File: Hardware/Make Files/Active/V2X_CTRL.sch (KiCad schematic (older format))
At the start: 37 parts, among them CON1 AVR-PDI-6, IC1 ATXMEGA16A4U-A, P20 Jumper 1, P21 Jumper 2, P22 CONN_02X04, P23 Jumper 3, P24 Jumper 4, Q16 2N7000, Q17 2N7000, Q18 2N7000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

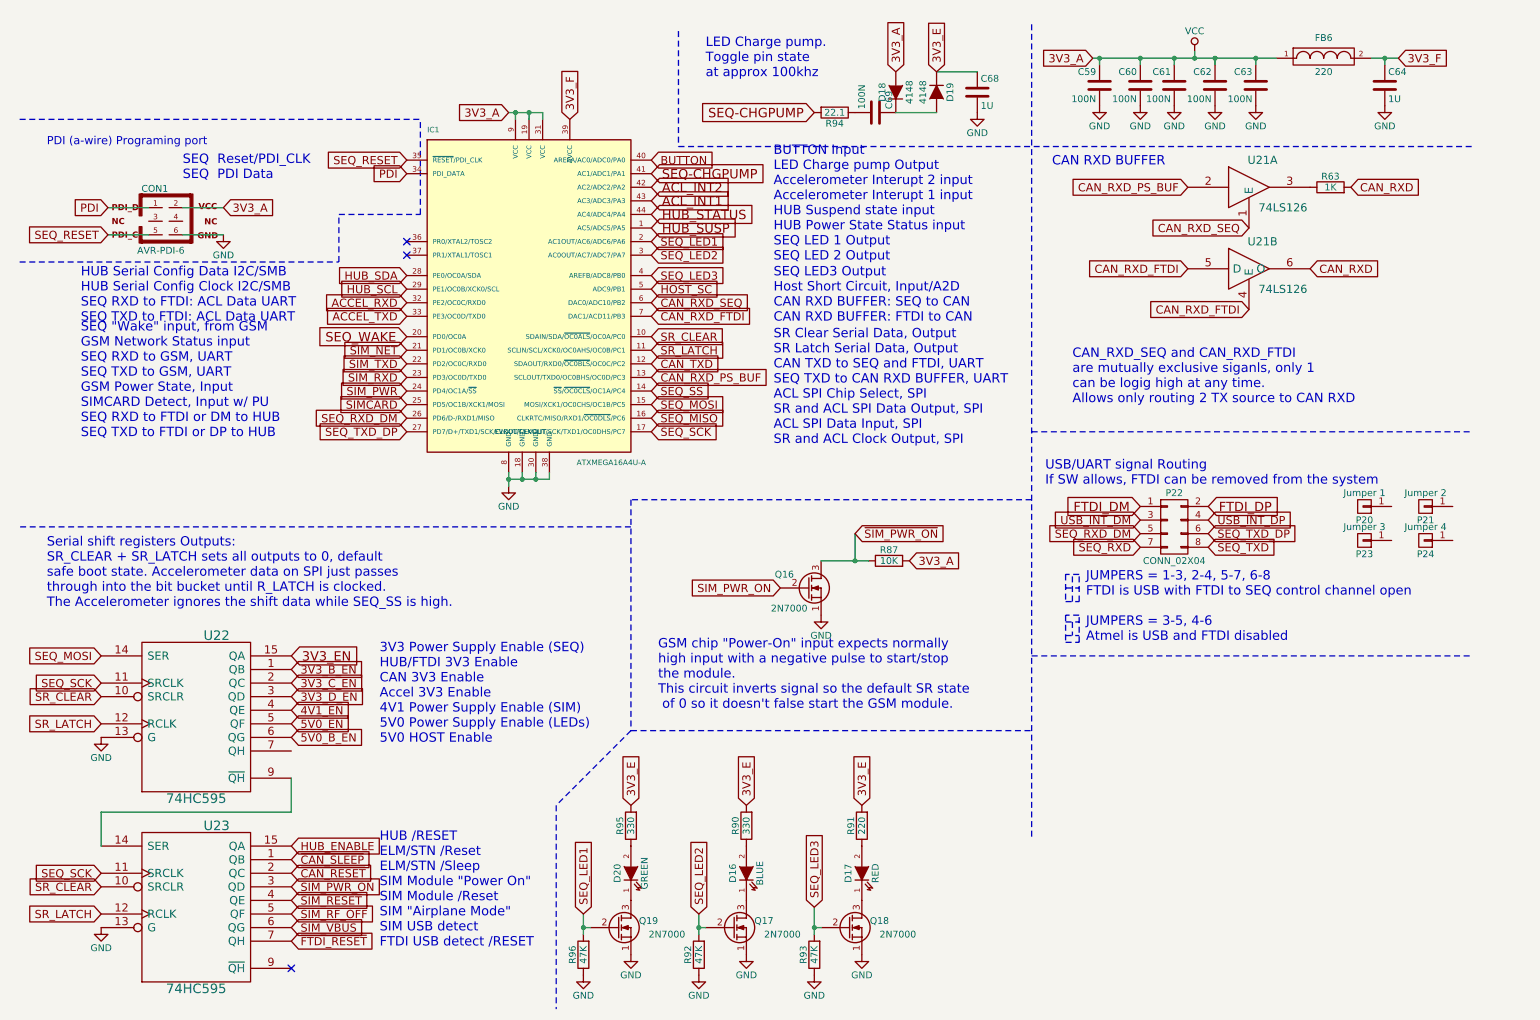
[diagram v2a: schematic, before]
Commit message: Verification findings and modifications
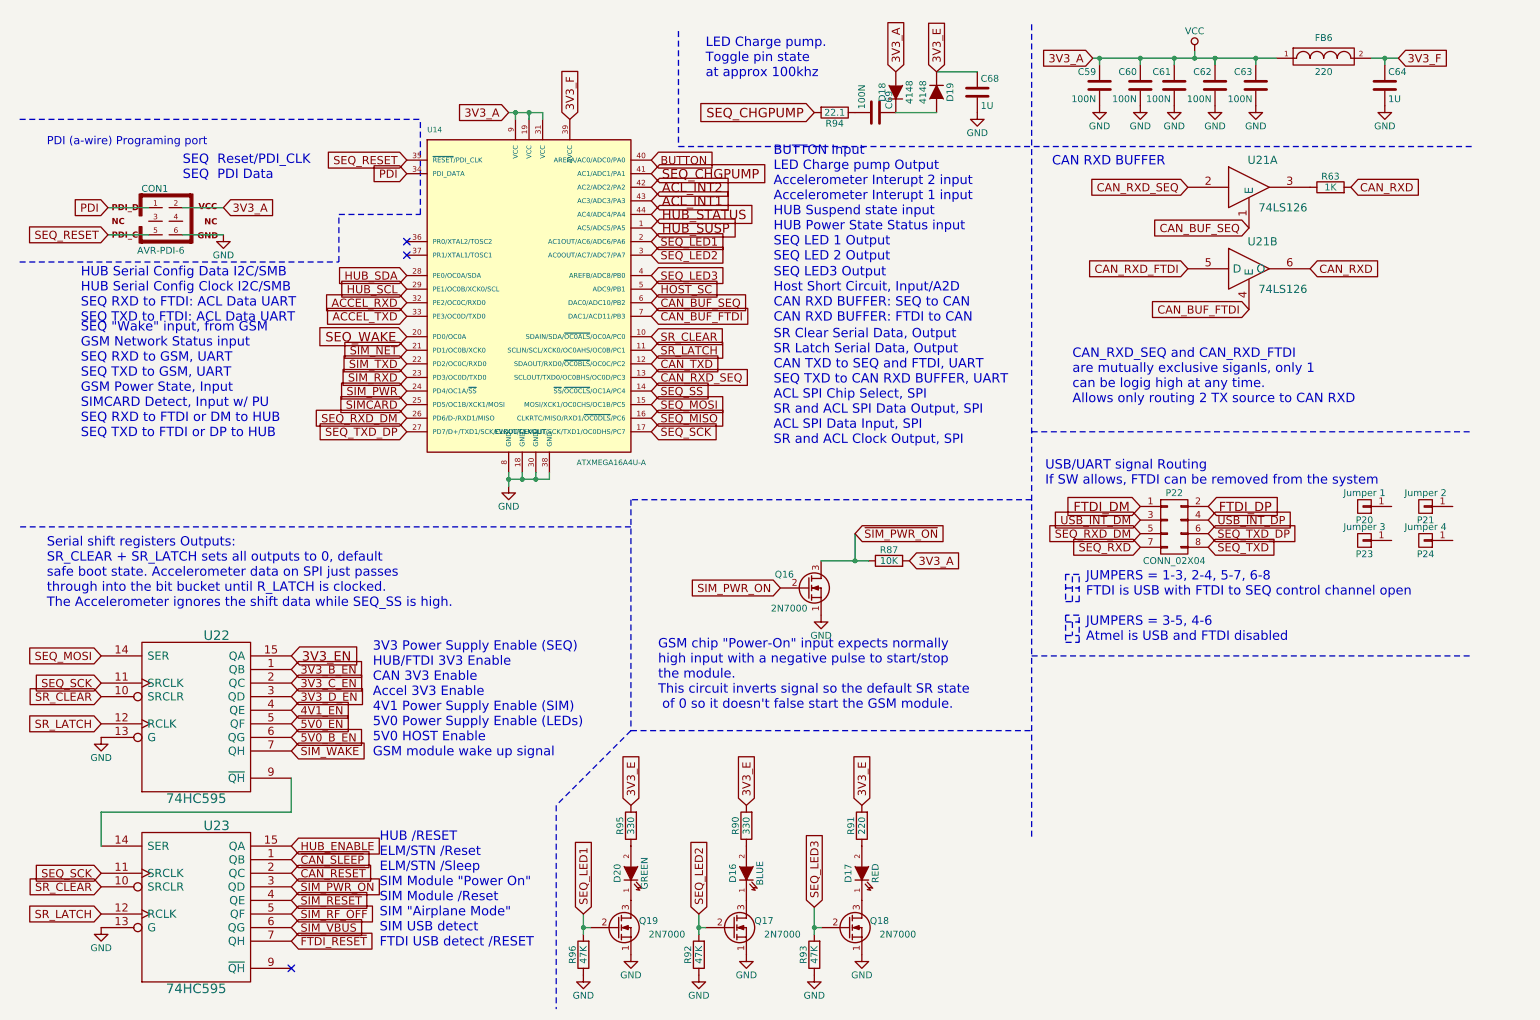
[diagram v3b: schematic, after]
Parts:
- CON1: footprint Pin_Headers:Pin_Header_Straight_2x03 -> Pin_Headers:Pin_Header_Angled_2x03
- renumbered IC1 to U14
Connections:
- net CAN_RXD_PS_BUF is gone; now on net CAN_RXD_SEQ: U14.13 (SCLOUT/TXD0/OC0BHS/OC0D/PC3), U21.2
- net CAN_RXD_FTDI: no longer U14.7 (DAC1/ACD11/PB3), U21.4 (E)
- net CAN_RXD_SEQ: no longer U14.6 (DAC0/ADC10/PB2), U21.1 (E)
- net SIM_WAKE: now reaches U22.7 (QH)
- net SEQ-CHGPUMP renamed SEQ_CHGPUMP
- new net CAN_BUF_FTDI: U14.7 (DAC1/ACD11/PB3), U21.4 (E)
- new net CAN_BUF_SEQ: U14.6 (DAC0/ADC10/PB2), U21.1 (E)
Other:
- note added: "3V3 Power Supply Enable (SEQ)\nHUB/FTDI 3V3 Enable\nCAN 3V3 Enable\nAccel 3V3 Enable\n4V1 Power Supply Enable (SIM)\n5V0 Power Supply Enable (LEDs)\n5V0 HOST Enable \nGSM module wake up signal"
- note removed: "3V3 Power Supply Enable (SEQ)\nHUB/FTDI 3V3 Enable\nCAN 3V3 Enable\nAccel 3V3 Enable\n4V1 Power Supply Enable (SIM)\n5V0 Power Supply Enable (LEDs)\n5V0 HOST Enable \n"
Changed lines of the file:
@@
 SEQ_LED2
 $Comp
-L GND #PWR96
+L GND #PWR092
 U 1 1 55F86E9C
 P 4100 3900
-F 0 "#PWR96" H 4100 3650 50  0001 C CNN
+F 0 "#PWR092" H 4100 3650 50  0001 C CNN
 F 1 "GND" H 4100 3750 50  0000 C CNN
 F 2 "" H 4100 3900 60  0000 C CNN
@@
 HOST_SC
 $Comp
-L ATXMEGA16A4U-A IC1
+L ATXMEGA16A4U-A U14
 U 1 1 55F86EE3
 P 4250 2500
-F 0 "IC1" H 3500 3700 40  0000 L BNN
+F 0 "U14" H 3500 3700 40  0000 L BNN
 F 1 "ATXMEGA16A4U-A" H 4600 1250 40  0000 L BNN
 F 2 "Housings_QFP:TQFP-44_10x10mm_Pitch0.8mm" H 4250 2500 35  0001 C CIN
@@
 PDI
 $Comp
-L GND #PWR95
+L GND #PWR093
 U 1 1 55F86EF0
 P 2000 2050
-F 0 "#PWR95" H 2000 1800 50  0001 C CNN
+F 0 "#PWR093" H 2000 1800 50  0001 C CNN
 F 1 "GND" H 2000 1900 50  0000 C CNN
 F 2 "" H 2000 2050 60  0000 C CNN
@@
 F 0 "CON1" H 1495 2190 50  0000 C CNN
 F 1 "AVR-PDI-6" H 1365 1705 50  0000 L BNN
-F 2 "Pin_Headers:Pin_Header_Straight_2x03" V 1130 1985 50  0001 C CNN
+F 2 "Pin_Headers:Pin_Header_Angled_2x03" V 1130 1985 50  0001 C CNN
 F 3 "http://www.mouser.com/ds/2/418/NG_CD_146130_L_146130_c.dwg-614944.pdf" H 1575 1950 60  0001 C CNN
 F 4 "571-5-146130-2" H 1575 1950 60  0001 C CNN "Mouse PN"
@@
 Text Notes 3150 7300 0    69   ~ 0
 HUB /RESET\nELM/STN /Reset\nELM/STN /Sleep\nSIM Module "Power On"\nSIM Module /Reset\nSIM "Airplane Mode"\nSIM USB detect\nFTDI USB detect /RESET
-Text Notes 3150 5800 0    69   ~ 0
-3V3 Power Supply Enable (SEQ)\nHUB/FTDI 3V3 Enable\nCAN 3V3 Enable\nAccel 3V3 Enable\n4V1 Power Supply Enable (SIM)\n5V0 Power Supply Enable (LEDs)\n5V0 HOST Enable \n
+Text Notes 3100 5900 0    69   ~ 0
+3V3 Power Supply Enable (SEQ)\nHUB/FTDI 3V3 Enable\nCAN 3V3 Enable\nAccel 3V3 Enable\n4V1 Power Supply Enable (SIM)\n5V0 Power Supply Enable (LEDs)\n5V0 HOST Enable \nGSM module wake up signal
 Text Notes 950  2700 0    69   ~ 0
 HUB Serial Config Data I2C/SMB\nHUB Serial Config Clock I2C/SMB\nSEQ RXD to FTDI: ACL Data UART\nSEQ TXD to FTDI: ACL Data UART
@@
 $EndComp
 Text GLabel 9100 1700 0    60   Input ~ 0
-CAN_RXD_PS_BUF
+CAN_RXD_SEQ
 Text GLabel 9100 2300 0    60   Input ~ 0
 CAN_RXD_FTDI
@@
 5V0_B_EN
 $Comp
-L GND #PWR93
+L GND #PWR094
 U 1 1 55FA434A
 P 1100 5750
-F 0 "#PWR93" H 1100 5500 50  0001 C CNN
+F 0 "#PWR094" H 1100 5500 50  0001 C CNN
 F 1 "GND" H 1100 5600 50  0000 C CNN
 F 2 "" H 1100 5750 60  0000 C CNN
@@
 $EndComp
 $Comp
-L GND #PWR94
+L GND #PWR095
 U 1 1 55FA46C8
 P 1100 7150
-F 0 "#PWR94" H 1100 6900 50  0001 C CNN
+F 0 "#PWR095" H 1100 6900 50  0001 C CNN
 F 1 "GND" H 1100 7000 50  0000 C CNN
 F 2 "" H 1100 7150 60  0000 C CNN
@@
 $EndComp
 $Comp
-L GND #PWR100
+L GND #PWR096
 U 1 1 55FD726F
 P 5850 7350
-F 0 "#PWR100" H 5850 7100 50  0001 C CNN
+F 0 "#PWR096" H 5850 7100 50  0001 C CNN
 F 1 "GND" H 5850 7200 50  0000 C CNN
 F 2 "" H 5850 7350 60  0000 C CNN
@@
 $EndComp
 $Comp
-L GND #PWR99
+L GND #PWR097
 U 1 1 55FD7284
 P 5500 7500
-F 0 "#PWR99" H 5500 7250 50  0001 C CNN
+F 0 "#PWR097" H 5500 7250 50  0001 C CNN
 F 1 "GND" H 5500 7350 50  0000 C CNN
 F 2 "" H 5500 7500 60  0000 C CNN
@@
 $EndComp
 $Comp
-L GND #PWR101
+L GND #PWR098
 U 1 1 55FD7672
 P 6350 7500
-F 0 "#PWR101" H 6350 7250 50  0001 C CNN
+F 0 "#PWR098" H 6350 7250 50  0001 C CNN
 F 1 "GND" H 6350 7350 50  0000 C CNN
 F 2 "" H 6350 7500 60  0000 C CNN
@@
 	6350 7000 6350 7200
 $Comp
-L GND #PWR103
+L GND #PWR099
 U 1 1 55FD7660
 P 6700 7350
-F 0 "#PWR103" H 6700 7100 50  0001 C CNN
+F 0 "#PWR099" H 6700 7100 50  0001 C CNN
 F 1 "GND" H 6700 7200 50  0000 C CNN
 F 2 "" H 6700 7350 60  0000 C CNN
@@
 $EndComp
 $Comp
-L GND #PWR102
+L GND #PWR0100
 U 1 1 55FE1020
 P 6400 4850
-F 0 "#PWR102" H 6400 4600 50  0001 C CNN
+F 0 "#PWR0100" H 6400 4600 50  0001 C CNN
 F 1 "GND" H 6400 4700 50  0000 C CNN
 F 2 "" H 6400 4850 60  0000 C CNN
@@
 Connection ~ 10550 750
 $Comp
-L GND #PWR111
+L GND #PWR0101
 U 1 1 56006FBB
 P 10550 1100
-F 0 "#PWR111" H 10550 850 50  0001 C CNN
+F 0 "#PWR0101" H 10550 850 50  0001 C CNN
 F 1 "GND" H 10550 950 50  0000 C CNN
 F 2 "" H 10550 1100 60  0000 C CNN
@@
 Connection ~ 9000 750
 $Comp
-L GND #PWR107
+L GND #PWR0102
 U 1 1 560285A0
 P 9000 1100
-F 0 "#PWR107" H 9000 850 50  0001 C CNN
+F 0 "#PWR0102" H 9000 850 50  0001 C CNN
 F 1 "GND" H 9000 950 50  0000 C CNN
 F 2 "" H 9000 1100 60  0000 C CNN
@@
 $EndComp
 $Comp
-L GND #PWR109
+L GND #PWR0103
 U 1 1 560285F6
 P 9300 1100
-F 0 "#PWR109" H 9300 850 50  0001 C CNN
+F 0 "#PWR0103" H 9300 850 50  0001 C CNN
 F 1 "GND" H 9300 950 50  0000 C CNN
 F 2 "" H 9300 1100 60  0000 C CNN
@@
 $EndComp
 $Comp
-L GND #PWR110
+L GND #PWR0104
 U 1 1 5602864C
 P 9600 1100
-F 0 "#PWR110" H 9600 850 50  0001 C CNN
+F 0 "#PWR0104" H 9600 850 50  0001 C CNN
 F 1 "GND" H 9600 950 50  0000 C CNN
 F 2 "" H 9600 1100 60  0000 C CNN
@@
 Connection ~ 9150 750
 $Comp
-L VCC #PWR108
+L VCC #PWR0105
 U 1 1 56029609
 P 9150 700
-F 0 "#PWR108" H 9150 550 50  0001 C CNN
+F 0 "#PWR0105" H 9150 550 50  0001 C CNN
 F 1 "VCC" H 9150 850 50  0000 C CNN
 F 2 "" H 9150 700 60  0000 C CNN
@@
 Connection ~ 8750 750
 $Comp
-L GND #PWR106
+L GND #PWR0106
 U 1 1 5602C4DB
 P 8750 1100
-F 0 "#PWR106" H 8750 850 50  0001 C CNN
+F 0 "#PWR0106" H 8750 850 50  0001 C CNN
 F 1 "GND" H 8750 950 50  0000 C CNN
 F 2 "" H 8750 1100 60  0000 C CNN
@@
 $EndComp
 $Comp
-L GND #PWR105
+L GND #PWR0107
 U 1 1 5602C537
 P 8450 1100
-F 0 "#PWR105" H 8450 850 50  0001 C CNN
+F 0 "#PWR0107" H 8450 850 50  0001 C CNN
 F 1 "GND" H 8450 950 50  0000 C CNN
 F 2 "" H 8450 1100 60  0000 C CNN
@@
 3V3_A
 Text GLabel 9550 2600 0    60   Input ~ 0
-CAN_RXD_FTDI
+CAN_BUF_FTDI
 Text GLabel 9550 2000 0    60   Input ~ 0
-CAN_RXD_SEQ
+CAN_BUF_SEQ
 Text GLabel 2500 5450 2    60   Input ~ 0
 3V3_D_EN
-Text GLabel 5150 2550 2    60   Input ~ 0
-CAN_RXD_SEQ
-Text GLabel 5150 2650 2    60   Input ~ 0
-CAN_RXD_FTDI
 Text GLabel 8750 4150 0    60   Input ~ 0
 USB_INT_DM
@@
 SEQ_LED3
 Text GLabel 5150 1600 2    69   Input ~ 0
-SEQ-CHGPUMP
+SEQ_CHGPUMP
 $Comp
 L LED D20
@@
 $EndComp
 $Comp
-L GND #PWR98
+L GND #PWR0108
 U 1 1 560D95B8
 P 5000 7350
-F 0 "#PWR98" H 5000 7100 50  0001 C CNN
+F 0 "#PWR0108" H 5000 7100 50  0001 C CNN
 F 1 "GND" H 5000 7200 50  0000 C CNN
 F 2 "" H 5000 7350 60  0000 C CNN
@@
 $EndComp
 $Comp
-L GND #PWR97
+L GND #PWR0109
 U 1 1 560D95C5
 P 4650 7500
-F 0 "#PWR97" H 4650 7250 50  0001 C CNN
+F 0 "#PWR0109" H 4650 7250 50  0001 C CNN
 F 1 "GND" H 4650 7350 50  0000 C CNN
 F 2 "" H 4650 7500 60  0000 C CNN
@@
 $EndComp
 Text GLabel 6350 1150 0    69   Input ~ 0
-SEQ-CHGPUMP
+SEQ_CHGPUMP
 $Comp
 L R R94
@@
 $EndComp
 $Comp
-L GND #PWR104
+L GND #PWR0110
 U 1 1 560DBE9F
 P 7550 1150
-F 0 "#PWR104" H 7550 900 50  0001 C CNN
+F 0 "#PWR0110" H 7550 900 50  0001 C CNN
 F 1 "GND" H 7550 1000 50  0000 C CNN
 F 2 "" H 7550 1150 60  0000 C CNN
@@
 Text GLabel 6350 7000 1    60   Input ~ 0
 SEQ_LED3
-Text GLabel 5150 3100 2    60   Input ~ 0
-CAN_RXD_PS_BUF
 Text Notes 8100 1550 0    69   ~ 0
 CAN RXD BUFFER
@@
 	0    -1   -1   0
 $EndComp
+Text GLabel 5150 2550 2    60   Input ~ 0
+CAN_BUF_SEQ
+Text GLabel 5150 2650 2    60   Input ~ 0
+CAN_BUF_FTDI
+Text GLabel 5150 3100 2    60   Input ~ 0
+CAN_RXD_SEQ
+Text GLabel 2500 5850 2    60   Input ~ 0
+SIM_WAKE
 $EndSCHEMATC

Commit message: V2X V1.2 PCB build, with shares
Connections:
- no-connect marks 3 -> 9
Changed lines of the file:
@@
 SEQ_LED2
 $Comp
-L GND #PWR092
+L GND #PWR094
 U 1 1 55F86E9C
 P 4100 3900
-F 0 "#PWR092" H 4100 3650 50  0001 C CNN
+F 0 "#PWR094" H 4100 3650 50  0001 C CNN
 F 1 "GND" H 4100 3750 50  0000 C CNN
 F 2 "" H 4100 3900 60  0000 C CNN
@@
 PDI
 $Comp
-L GND #PWR093
+L GND #PWR095
 U 1 1 55F86EF0
 P 2000 2050
-F 0 "#PWR093" H 2000 1800 50  0001 C CNN
+F 0 "#PWR095" H 2000 1800 50  0001 C CNN
 F 1 "GND" H 2000 1900 50  0000 C CNN
 F 2 "" H 2000 2050 60  0000 C CNN
@@
 5V0_B_EN
 $Comp
-L GND #PWR094
+L GND #PWR096
 U 1 1 55FA434A
 P 1100 5750
-F 0 "#PWR094" H 1100 5500 50  0001 C CNN
+F 0 "#PWR096" H 1100 5500 50  0001 C CNN
 F 1 "GND" H 1100 5600 50  0000 C CNN
 F 2 "" H 1100 5750 60  0000 C CNN
@@
 $EndComp
 $Comp
-L GND #PWR095
+L GND #PWR097
 U 1 1 55FA46C8
 P 1100 7150
-F 0 "#PWR095" H 1100 6900 50  0001 C CNN
+F 0 "#PWR097" H 1100 6900 50  0001 C CNN
 F 1 "GND" H 1100 7000 50  0000 C CNN
 F 2 "" H 1100 7150 60  0000 C CNN
@@
 $EndComp
 $Comp
-L GND #PWR096
+L GND #PWR098
 U 1 1 55FD726F
 P 5850 7350
-F 0 "#PWR096" H 5850 7100 50  0001 C CNN
+F 0 "#PWR098" H 5850 7100 50  0001 C CNN
 F 1 "GND" H 5850 7200 50  0000 C CNN
 F 2 "" H 5850 7350 60  0000 C CNN
@@
 $EndComp
 $Comp
-L GND #PWR097
+L GND #PWR099
 U 1 1 55FD7284
 P 5500 7500
-F 0 "#PWR097" H 5500 7250 50  0001 C CNN
+F 0 "#PWR099" H 5500 7250 50  0001 C CNN
 F 1 "GND" H 5500 7350 50  0000 C CNN
 F 2 "" H 5500 7500 60  0000 C CNN
@@
 $EndComp
 $Comp
-L GND #PWR098
+L GND #PWR0100
 U 1 1 55FD7672
 P 6350 7500
-F 0 "#PWR098" H 6350 7250 50  0001 C CNN
+F 0 "#PWR0100" H 6350 7250 50  0001 C CNN
 F 1 "GND" H 6350 7350 50  0000 C CNN
 F 2 "" H 6350 7500 60  0000 C CNN
@@
 	6350 7000 6350 7200
 $Comp
-L GND #PWR099
+L GND #PWR0101
 U 1 1 55FD7660
 P 6700 7350
-F 0 "#PWR099" H 6700 7100 50  0001 C CNN
+F 0 "#PWR0101" H 6700 7100 50  0001 C CNN
 F 1 "GND" H 6700 7200 50  0000 C CNN
 F 2 "" H 6700 7350 60  0000 C CNN
@@
 $EndComp
 $Comp
-L GND #PWR0100
+L GND #PWR0102
 U 1 1 55FE1020
 P 6400 4850
-F 0 "#PWR0100" H 6400 4600 50  0001 C CNN
+F 0 "#PWR0102" H 6400 4600 50  0001 C CNN
 F 1 "GND" H 6400 4700 50  0000 C CNN
 F 2 "" H 6400 4850 60  0000 C CNN
@@
 Connection ~ 10550 750
 $Comp
-L GND #PWR0101
+L GND #PWR0103
 U 1 1 56006FBB
 P 10550 1100
-F 0 "#PWR0101" H 10550 850 50  0001 C CNN
+F 0 "#PWR0103" H 10550 850 50  0001 C CNN
 F 1 "GND" H 10550 950 50  0000 C CNN
 F 2 "" H 10550 1100 60  0000 C CNN
@@
 Connection ~ 9000 750
 $Comp
-L GND #PWR0102
+L GND #PWR0104
 U 1 1 560285A0
 P 9000 1100
-F 0 "#PWR0102" H 9000 850 50  0001 C CNN
+F 0 "#PWR0104" H 9000 850 50  0001 C CNN
 F 1 "GND" H 9000 950 50  0000 C CNN
 F 2 "" H 9000 1100 60  0000 C CNN
@@
 $EndComp
 $Comp
-L GND #PWR0103
+L GND #PWR0105
 U 1 1 560285F6
 P 9300 1100
-F 0 "#PWR0103" H 9300 850 50  0001 C CNN
+F 0 "#PWR0105" H 9300 850 50  0001 C CNN
 F 1 "GND" H 9300 950 50  0000 C CNN
 F 2 "" H 9300 1100 60  0000 C CNN
@@
 $EndComp
 $Comp
-L GND #PWR0104
+L GND #PWR0106
 U 1 1 5602864C
 P 9600 1100
-F 0 "#PWR0104" H 9600 850 50  0001 C CNN
+F 0 "#PWR0106" H 9600 850 50  0001 C CNN
 F 1 "GND" H 9600 950 50  0000 C CNN
 F 2 "" H 9600 1100 60  0000 C CNN
@@
 Connection ~ 9150 750
 $Comp
-L VCC #PWR0105
+L VCC #PWR0107
 U 1 1 56029609
 P 9150 700
-F 0 "#PWR0105" H 9150 550 50  0001 C CNN
+F 0 "#PWR0107" H 9150 550 50  0001 C CNN
 F 1 "VCC" H 9150 850 50  0000 C CNN
 F 2 "" H 9150 700 60  0000 C CNN
@@
 Connection ~ 8750 750
 $Comp
-L GND #PWR0106
+L GND #PWR0108
 U 1 1 5602C4DB
 P 8750 1100
-F 0 "#PWR0106" H 8750 850 50  0001 C CNN
+F 0 "#PWR0108" H 8750 850 50  0001 C CNN
 F 1 "GND" H 8750 950 50  0000 C CNN
 F 2 "" H 8750 1100 60  0000 C CNN
@@
 $EndComp
 $Comp
-L GND #PWR0107
+L GND #PWR0109
 U 1 1 5602C537
 P 8450 1100
-F 0 "#PWR0107" H 8450 850 50  0001 C CNN
+F 0 "#PWR0109" H 8450 850 50  0001 C CNN
 F 1 "GND" H 8450 950 50  0000 C CNN
 F 2 "" H 8450 1100 60  0000 C CNN
@@
 $EndComp
 $Comp
-L GND #PWR0108
+L GND #PWR0110
 U 1 1 560D95B8
 P 5000 7350
-F 0 "#PWR0108" H 5000 7100 50  0001 C CNN
+F 0 "#PWR0110" H 5000 7100 50  0001 C CNN
 F 1 "GND" H 5000 7200 50  0000 C CNN
 F 2 "" H 5000 7350 60  0000 C CNN
@@
 $EndComp
 $Comp
-L GND #PWR0109
+L GND #PWR0111
 U 1 1 560D95C5
 P 4650 7500
-F 0 "#PWR0109" H 4650 7250 50  0001 C CNN
+F 0 "#PWR0111" H 4650 7250 50  0001 C CNN
 F 1 "GND" H 4650 7350 50  0000 C CNN
 F 2 "" H 4650 7500 60  0000 C CNN
@@
 $EndComp
 $Comp
-L GND #PWR0110
+L GND #PWR0112
 U 1 1 560DBE9F
 P 7550 1150
-F 0 "#PWR0110" H 7550 900 50  0001 C CNN
+F 0 "#PWR0112" H 7550 900 50  0001 C CNN
 F 1 "GND" H 7550 1000 50  0000 C CNN
 F 2 "" H 7550 1150 60  0000 C CNN
@@
 Text GLabel 2500 5850 2    60   Input ~ 0
 SIM_WAKE
+NoConn ~ 1450 1950
+NoConn ~ 1700 1950
+NoConn ~ 10600 4050
+NoConn ~ 10600 4300
+NoConn ~ 11050 4050
+NoConn ~ 11050 4300
 $EndSCHEMATC

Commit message: BOM updates
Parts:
- R91: value 220 -> 330; Mouse PN 71-CRCW0603-220-E3 -> 71-CRCW0603-330-E3
- R94: value 22.1 -> 22
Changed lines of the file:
@@
-$EndComp
-$Comp
-L R R91
-U 1 1 55FD7666
-P 6700 6400
-F 0 "R91" V 6780 6400 50  0000 C CNN
-F 1 "220" V 6700 6400 50  0000 C CNN
-F 2 "Custom Parts:R_0603_sm" V 6630 6400 30  0001 C CNN
-F 3 "http://www.mouser.com/ds/2/427/dcrcwe3-109170.pdf" H 6700 6400 30  0001 C CNN
-F 4 "71-CRCW0603-220-E3" H 6700 6400 60  0001 C CNN "Mouse PN"
-	1    6700 6400
-	-1   0    0    1
 $EndComp
 $Comp
@@
 P 6500 1150
 F 0 "R94" V 6580 1150 50  0000 C CNN
-F 1 "22.1" V 6500 1150 50  0000 C CNN
+F 1 "22" V 6500 1150 50  0000 C CNN
 F 2 "Custom Parts:R_0603_sm" V 6430 1150 30  0001 C CNN
 F 3 "http://www.vishay.com/doc?20035" H 6500 1150 30  0001 C CNN
@@
 NoConn ~ 11050 4050
 NoConn ~ 11050 4300
+$Comp
+L R R91
+U 1 1 562AAD52
+P 6700 6400
+F 0 "R91" V 6780 6400 50  0000 C CNN
+F 1 "330" V 6700 6400 50  0000 C CNN
+F 2 "Custom Parts:R_0603_sm" V 6630 6400 30  0001 C CNN
+F 3 "http://www.mouser.com/ds/2/427/dcrcwe3-109170.pdf" H 6700 6400 30  0001 C CNN
+F 4 "71-CRCW0603-330-E3" H 6700 6400 60  0001 C CNN "Mouse PN"
+	1    6700 6400
+	-1   0    0    1
+$EndComp
 $EndSCHEMATC
